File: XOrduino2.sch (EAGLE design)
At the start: 82 parts, among them J1 2.5mm, J2 2.5mm, J3 2.5mm, J4 2.5mm, J5 Batt In, J6 MOT R, J7 MOT L, P1 10k, Q1 ALS-PT204-6C/L177, SW1 RESET, SW2 6mm Button, SW3 LEFT BUMPER, SW4 RIGHT BUMPER, U1 ATMEGA32U4-XUAU, U2 LMV358, U3 NJU7261, U4 DRV8833PWP, U5 QRE1113GR, U6 QRE1113GR, X1 USBPCB, X2 USBMINIB, X3 USBMICROB-VIA, Y1 16MHz

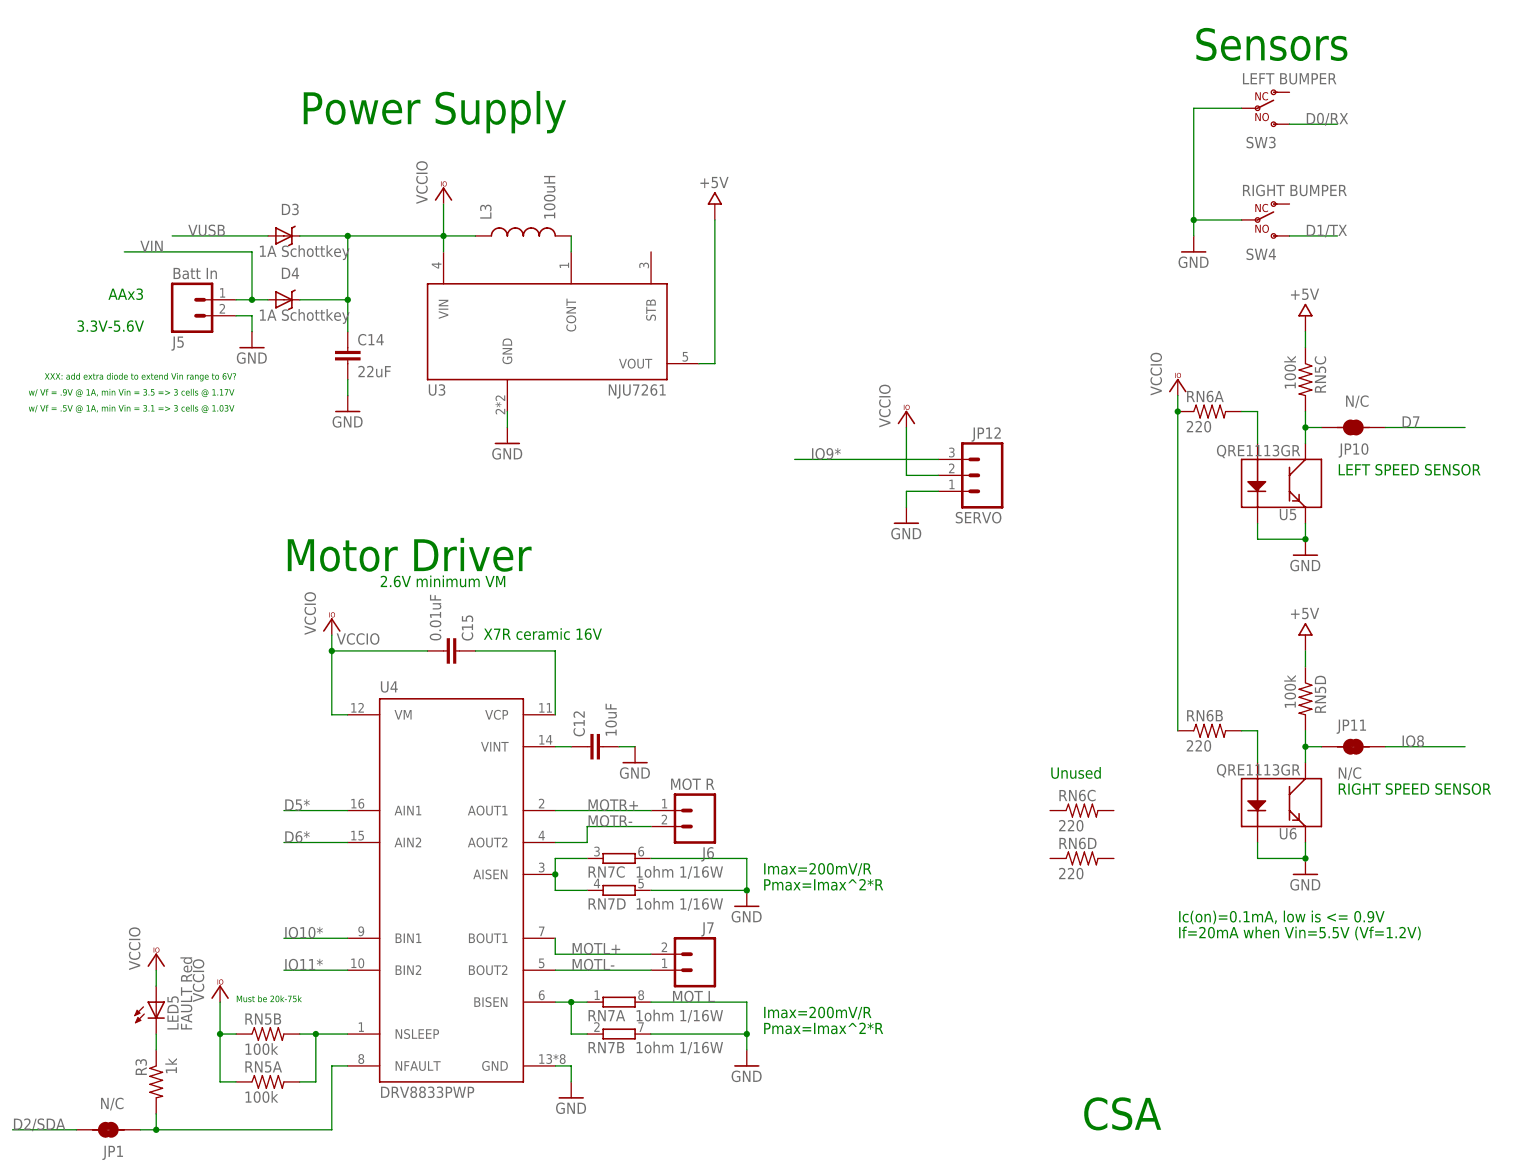
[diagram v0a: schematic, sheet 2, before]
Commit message: all of second page deleted
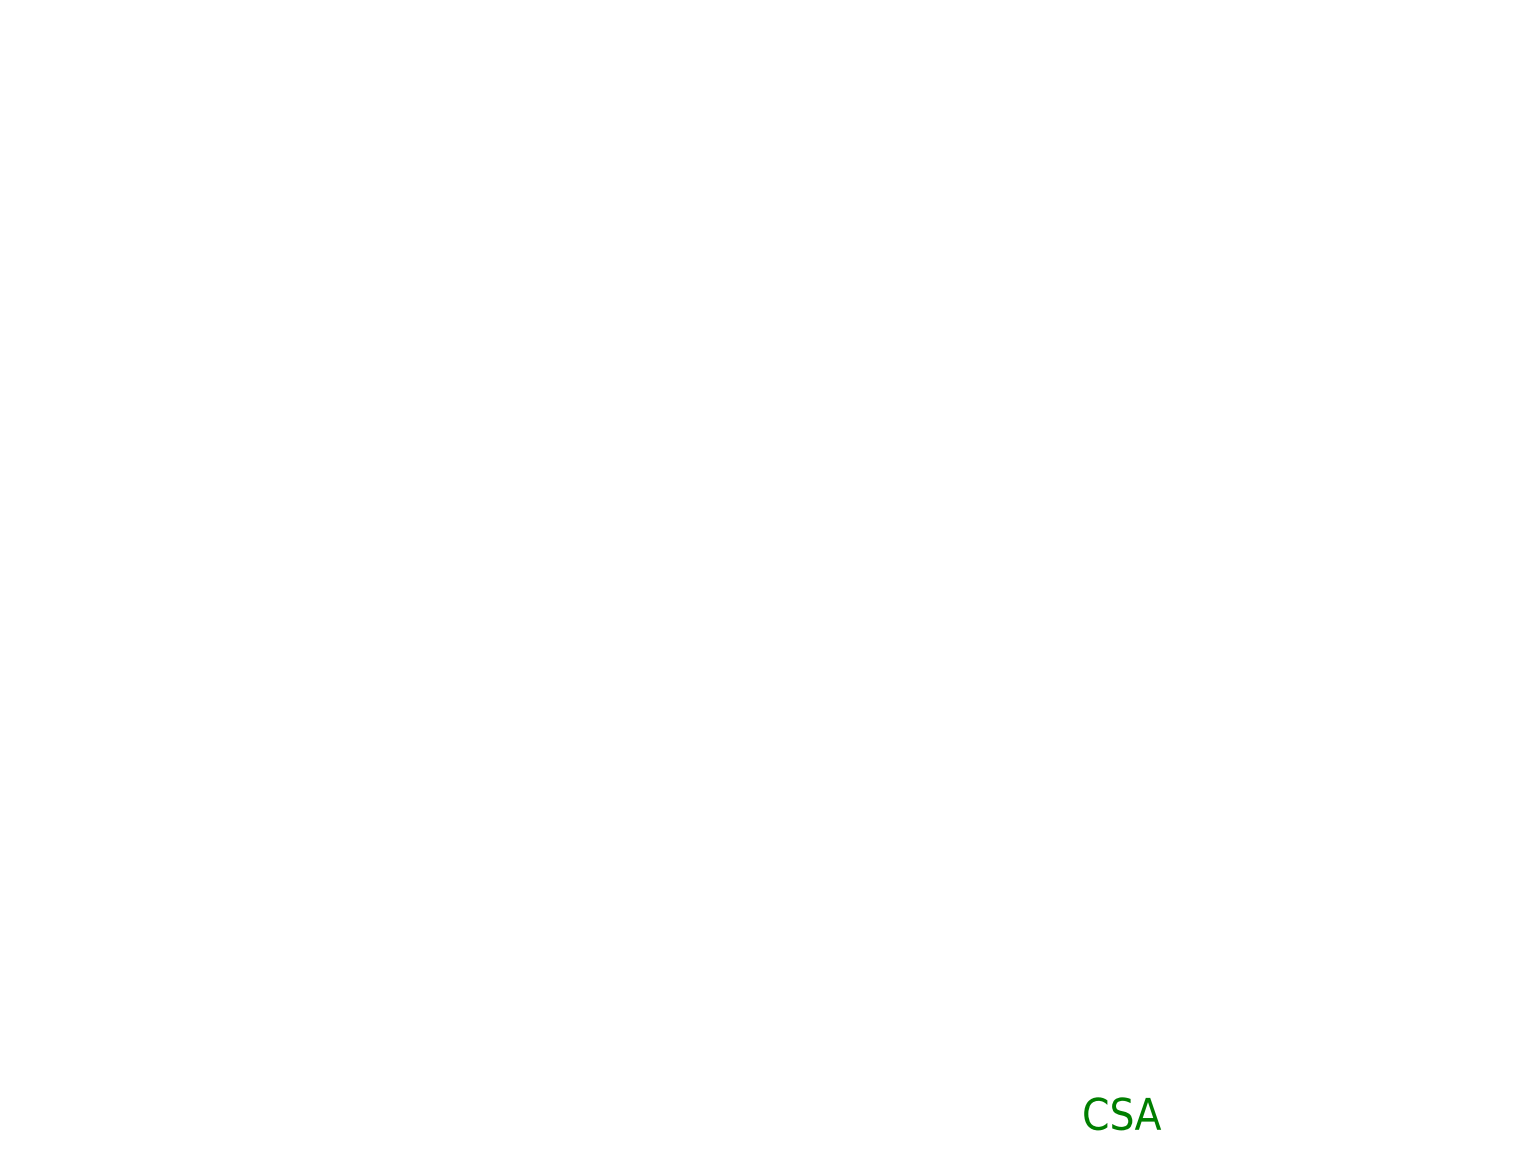
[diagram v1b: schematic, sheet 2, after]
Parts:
- removed C10: 0.22uF, SparkFun-Passives:CAP0805
- removed C11: 0.33uF, SparkFun-Passives:CAP0805
- removed C12: 10uF, SparkFun-Passives:CAP0805
- removed C14: 22uF, SparkFun-Passives:CAP1206
- removed C15: 0.01uF, SparkFun-Passives:CAP0805
- removed C7: 100n, SparkFun-Passives:CAP0805
- removed D1: 1N4148, SparkFun-DiscreteSemi:DIODE1N4148
- removed D3, D4: 1A Schottkey, SparkFun-DiscreteSemi:DIODE-SCHOTTKY_
- removed J1, J2, J3, J4: 2.5mm, xorduino:AUDIO-JACK
- removed J5: Batt In, SparkFun-Connectors:M02PTH
- removed J6: MOT R, SparkFun:M023.5MM
- removed J7: MOT L, SparkFun:M023.5MM
- removed JP1: N/C, xorduino:SOLDERJUMPERNOCONFLICT
- removed JP10, JP11: N/C, xorduino:SOLDERJUMPERBOT-VIA-NOCONFLICT
- removed JP12: SERVO, SparkFun-Connectors:M03PTH
- removed L3: 100uH, SparkFun-Passives:INDUCTOR1007
- removed LED5: FAULT Red, xorduino:LED0805
- removed MIC1: MIC9.7MM, SparkFun:MIC9.7MM
- removed P1: 10k, xorduino:POT
- removed Q1: ALS-PT204-6C/L177, xorduino:ALS-PT204-6C/L177
- removed R2: 2.2k, SparkFun-Passives:RESISTOR0805-RES
- removed R3: 1k, SparkFun-Passives:RESISTOR0805-RES
- removed RN5: 100k, xorduino:RESISTOR-ARRAYCRA06S
- removed RN6: 220, xorduino:RESISTOR-ARRAYCRA06S
- removed RN7: 1ohm 1/16W, resistor-dil:4R-NEXB38V
- removed SW2: 6mm Button, SparkFun-Electromechanical:TAC_SWITCHPTH
- removed SW3: LEFT BUMPER, xorduino:SWITCH-SPDTV1-NOHOLES
- removed SW4: RIGHT BUMPER, xorduino:SWITCH-SPDTV2-NOHOLES
- removed U3: NJU7261, xorduino:NJU7261
- removed U4: DRV8833PWP, xorduino:DRV8833PWP
- removed U5, U6: QRE1113GR, xorduino:QRE1113GR
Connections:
- removed net LED5_CATHODE: LED5.C, R3.1
- removed net MIC_IN: C7.1, MIC1.1, RN2B.1
- removed net MOTL+: J7.2, U4.BOUT1
- removed net MOTL-: J7.1, U4.BOUT2
- removed net MOTR+: J6.1, U4.AOUT1
- removed net MOTR-: J6.2, U4.AOUT2
- removed net OPAMP1_M: R2.2, RN4C.2, U2G$2.-IN2
- removed net OPAMP1_OUT: D1.A, RN4C.1, U2G$2.OUT2
- removed net OPAMP1_P: C7.2, RN2C.2, U2G$2.+IN2
- removed net U3_CONT: L3.2, U3.CONT
- removed net U4_AISEN: RN7C.1, RN7D.1, U4.AISEN
- removed net U4_BISEN: RN7A.1, RN7B.1, U4.BISEN
- removed net U4_NFAULT: JP1.1, R3.2, U4.NFAULT
- removed net U4_NSLEEP: RN5A.2, RN5B.2, U4.NSLEEP
- removed net U4_VCP: C15.1, U4.VCP
- removed net U4_VINT: C12.1, U4.VINT
- removed net U5_ANODE: RN6A.2, U5.A
- removed net U5_COLLECTOR: JP10.2, RN5C.2, U5.C
- removed net U6_ANODE: RN6B.2, U6.A
- removed net U6_COLLECTOR: JP11.1, RN5D.2, U6.C
- removed net VCCIO: C14.1, C15.2, D3.C, D4.C, JP12.2, L3.1, LED5.A, RN5A.1, RN5B.1, RN6A.1, RN6B.1, U3.VIN, U4.VM
- net +5V: no longer C11.1, P1.E, RN2B.2, RN4D.2, RN5C.1, RN5D.1, U3.VOUT
- net A0: no longer J1.TIP
- net A1: no longer J2.TIP
- net A2: no longer J3.TIP
- net A3: no longer J4.TIP
- net D0/RX: no longer SW3.NO
- net D1/TX: no longer SW4.NO
- net D2/SDA: no longer JP1.2
- net D5*: no longer U4.AIN1
- net D6*: no longer U4.AIN2
- net D7: no longer JP10.1
- net GND: no longer C10.1, C12.2, C14.2, J1.SLEEVE, J2.SLEEVE, J3.SLEEVE, J4.SLEEVE, J5.2, JP12.1, MIC1.2, P1.A, Q1.E1, R2.1, RN2C.1, RN4B.2, RN7A.2, RN7B.2, RN7C.2, RN7D.2, SW2.4, SW3.C, SW4.C, U3.GND, U4.GND, U5.E, U5.K, U6.E, U6.K
- net IO10*: no longer U4.BIN1
- net IO11*: no longer U4.BIN2
- net IO12: no longer SW2.1
- net IO8: no longer JP11.2
- net IO9*: no longer JP12.3
- net LIGHT: no longer C11.2, Q1.C1, RN4D.1
- net SLIDER: no longer P1.S
- net SOUND: no longer C10.2, D1.C, RN4B.1
- net VIN: no longer D4.A, J5.1
- net VUSB: no longer D3.A
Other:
- note removed: "2.6V minimum VM"
- note removed: "3.3V-5.6V"
- note removed: "A"
- note removed: "AAx3"
- note removed: "All components optional"
- note removed: "B"
- note removed: "C"
- note removed: "D"
- note removed: "Ic(on)=0.1mA, low is <= 0.9V"
- note removed: "If=20mA when Vin=5.5V (Vf=1.2V)"
- note removed: "Imax=200mV/R"
- note removed: "LEFT SPEED SENSOR"
- note removed: "LMV358"
- note removed: "Motor Driver"
- note removed: "Must be 20k-75k"
- note removed: "Pmax=Imax^2*R"
- note removed: "Power Supply"
- note removed: "RIGHT SPEED SENSOR"
- note removed: "Scratch Sensor Board"
- note removed: "Sensors"
- note removed: "X7R ceramic 16V"
- note removed: "XXX: add extra diode to extend Vin range to 6V?"
- note removed: "w/ Vf = .5V @ 1A, min Vin = 3.1 => 3 cells @ 1.03V"
- note removed: "w/ Vf = .9V @ 1A, min Vin = 3.5 => 3 cells @ 1.17V"

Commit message: most of un-needed items removed. Current sense mostly in place
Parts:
- removed H1: 10x1F-H8.5, SmartPrj:PINHD-1X10
- removed H2, H3: 8x1F-H8.5, SmartPrj:PINHD-1X8
- removed H4: 6x1F-H8.5, SmartPrj:PINHD-1X6
- removed JP5: N/C, xorduino:SOLDERJUMPERNOCONFLICT
- removed JP7, JP8: N/C, xorduino:SOLDERJUMPERBOT-VIA-NOCONFLICT
- removed JP9: N/C, xorduino:SOLDERJUMPERBOT-NOCONFLICT
- removed LED1: L Yellow, xorduino:LED0805
- removed U$5: OSHW-LOGOL, SparkFun-Aesthetics:OSHW-LOGOL
- removed X1: USBPCB, SparkFun-Connectors:USBPCB
- removed X2: USBMINIB, xorduino:USBMINIB
- U2: value LMV358 -> LCD-16X2SILK; device SparkFun:LMV358 -> SparkFun-Displays:LCD-16X2SILK
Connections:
- removed net +3V3: H3.4
- removed net IO13_MIRROR: JP5.2, RN3A.2, U2G$1.-IN1, U2G$1.OUT1
- removed net LED1_ANODE: LED1.A, RN3A.1
- removed net LIGHT: JP8.1
- removed net SLIDER: JP9.1
- removed net SOUND: JP7.1
- removed net VIN: H3.8
- net +5V: no longer H3.2, H3.5, U2G$1.+V
- net A0: no longer H4.1
- net A1: no longer H4.2
- net A2: no longer H4.3
- net A3: no longer H4.4
- net A4: no longer H4.5, JP7.2
- net A5: no longer H4.6, JP8.2
- net AREF: no longer H1.8
- net D0/RX: no longer H2.1
- net D1/TX: no longer H2.2
- net D2/SDA: no longer H1.9, H2.3
- net D3/SCL: no longer H1.10, H2.4
- net D4: no longer H2.5, JP9.2
- net D5*: no longer H2.6
- net D6*: no longer H2.7
- net D7: no longer H2.8
- net D_M: no longer X1.D-, X2.D-
- net D_P: no longer X1.D+, X2.D+
- net GND: no longer H1.7, H3.6, H3.7, LED1.C, U2G$1.GND
- net IO10*: no longer H1.3
- net IO11*: no longer H1.4
- net IO12: no longer H1.5
- net IO13*: no longer H1.6, JP5.1, U2G$1.+IN1
- net IO8: no longer H1.1
- net IO9*: no longer H1.2
- net RESET: no longer H3.3
- net UGND: no longer X1.GND, X2.GND
- net XUSB: no longer X1.VBUS, X2.VBUS
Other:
- note removed: "#PWM 10bit"
- note removed: "#PWM 16bit"
- note removed: "#PWM 8/16bit"
- note removed: "#PWM 8bit"
- note removed: "#PWM Hi-Speed"
- note removed: "+A10"
- note removed: "+A11"
- note removed: "+A6"
- note removed: "+A7"
- note removed: "+A8"
- note removed: "+A9"
- note removed: "+AIN0"
- note removed: "+PWM COMPL IO10"
- note removed: "10#"
- note removed: "11#"
- note removed: "3#"
- note removed: "5#"
- note removed: "6#"
- note removed: "9#"
- note removed: "ALT1"
- note removed: "ALT2"
- note removed: "ALT3"
- note removed: "Cut jumper if U2 populated"
- note removed: "IO"
- note removed: "IOREF"
- note removed: "PWM 16bit COMPL D6"
- note removed: "RFU"
- note removed: "TO ICSP"

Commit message: starting to eliminate vias, work with component orientation
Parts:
- removed D2: 1N4148, SparkFun-DiscreteSemi:DIODE1N4148
- removed F1: 0ZCC0110FF2C 1.1A, rcl:L-EUL1812
- removed JP2, JP3, JP4, JP6: N/C, xorduino:SOLDERJUMPERNOCONFLICT
- removed LED2: TX Red, xorduino:LED0805
- removed LED3: RX Red, xorduino:LED0805
- added Q1: 2N2907, adafruit:2N2907
- added R2, R3, R5, R6: (no value), SparkFun-Passives:RESISTOR1206
- added RN5: 22, xorduino:RESISTOR-ARRAYCRA06S
- added SW2: RESET, SparkFun-Electromechanical:TAC_SWITCHPTH
- added U$2: LMV358, SparkFun-AnalogIC:LMV358
- added U$5: MMDT3904, SparkFun-DiscreteSemi:MMDT3904
- added U$6: RJ45-8PTH, SparkFun-Connectors:RJ45-8PTH
- added U$8: LM2931_FIXED, SparkFun-PowerIC:LM2931_FIXED
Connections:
- removed net VUSB: F1.1, JP6.1, U1.VBUS
- removed net XUSB: F1.2, X3.VBUS
- new net N$1: RN5D.2, U$2G$1.+IN1, U$5G$1.C
- new net N$12: R5.2, U2.VO
- new net N$13: U2.A
- new net N$14: Q1.B, R6.2
- new net N$18: U$6.2, U$8.VIN
- new net N$2: RN5A.2, U$2G$2.-IN2
- new net N$3: RN5B.2, U$2G$2.+IN2, U$5G$2.C
- new net N$4: U$2G$1.OUT1, U$5G$1.B
- new net N$5: U$2G$2.OUT2, U$5G$2.B
- new net N$6: RN5C.2, U$2G$1.-IN1
- new net N$7: RN5A.1, RN5D.1, U$6.8
- new net N$8: RN5B.1, RN5C.1, U$6.7
- net +5V: now also Q1.E, U$8.VOUT, U1.VBUS, U2.VDD, X3.VBUS; no longer D2.C, JP2.1, JP6.2
- net A0: now also R3.2, U$5G$2.E
- net A1: now also R2.2, U$5G$1.E
- net AGND: no longer C6.1, JP3.1
- net AVCC: no longer JP2.2
- net D0/RX: now also U2.DB5
- net D1/TX: now also U2.DB4
- net D2/SDA: now also U2.DB6
- net D3/SCL: now also U2.DB7
- net GND: now also C6.1, R2.1, R3.1, R5.1, U$6.1, U$8.GND, U2.K, U2.R/W, U2.VSS; no longer JP3.2, JP4.1
- net LED2_ANODE: no longer LED2.A
- net LED3_ANODE: no longer LED3.A
- net RESET: no longer D2.A
- net RXLED: no longer LED3.C
- net TXLED: no longer LED2.C
- net UGND: no longer JP4.2
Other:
- note added: "Battery Monitor"
- note removed: "0"
- note removed: "1"
- note removed: "10"
- note removed: "11"
- note removed: "12"
- note removed: "13"
- note removed: "2"
- note removed: "3"
- note removed: "4"
- note removed: "5"
- note removed: "6"
- note removed: "7"
- note removed: "9"
- note removed: "XOrduino2 (leonardo-compatible)"
- moved on the sheet: L2, RN1A, RN1B, RN1C, RN1D, RN4A, Z1, Z2

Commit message: changed usb connector, most of the devices are connected
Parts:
- removed R3: (no value), SparkFun-Passives:RESISTOR1206
- removed RN4: 100k, xorduino:RESISTOR-ARRAYCRA06S
- removed X3: USBMICROB-VIA, xorduino:USBMICROB-VIA
- added JP1: USB-RECEPTABLE, daspilker:USB-RECEPTABLE
- added R4, R7: (no value), SparkFun-Passives:RESISTOR0805-RES
- added RN6: 10k, xorduino:RESISTOR-ARRAYCRA06S
- R2: device SparkFun-Passives:RESISTOR1206 -> SparkFun-Passives:RESISTOR0805-RES
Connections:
- removed net A1: R2.2, U$5G$1.E, U1.(ADC6/TDO)PF6
- removed net LED2_ANODE: RN3C.1
- new net N$11: R2.1, RN3C.2, U1.(ADC7/TDI)PF7
- new net N$15: JP1.ID
- new net N$9: U1.(ADC5/TMS)PF5
- net +5V: now also JP1.VCC, RN6A.2, RN6B.2; no longer RN2A.2, RN3C.2, X3.VBUS
- net A0: now also R7.2, U1.(ADC6/TDO)PF6; no longer R3.2, U1.(ADC7/TDI)PF7
- net A2: now also R4.2, U$5G$1.E; no longer U1.(ADC5/TMS)PF5
- net D7: now also RN6B.1, SW2.4
- net D_M: now also JP1.D-, RN1D.2; no longer RN1C.2, X3.D-
- net D_P: now also JP1.D+, RN1C.2; no longer RN1D.2, X3.D+
- net GND: now also R4.1, R7.1, RN3C.1, SW2.2; no longer R2.1, R3.1
- net N$7: now also R2.2
- net RD_M: now also RN1D.1; no longer RN1C.1
- net RD_P: now also RN1C.1; no longer RN1D.1
- net RESET: now also RN6A.1; no longer RN2A.1
- net UGND: now also JP1.GND; no longer X3.GND
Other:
- note removed: "Cut for Battery Power Option"
- moved on the sheet: C8, L2, R2, RN1C, RN1D, RN3C, Z1, Z2

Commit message: added terminal block to sense power on
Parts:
- removed RN2: 10k, xorduino:RESISTOR-ARRAYCRA06S
- added C10, C7: (no value), SparkFun-Capacitors:CAP0805
- added R3: (no value), adafruit:R-US_0207/15
- added X1: (no value), con-wago-508:W237-03P
- RN5: value 22 -> 1K
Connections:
- new net N$10: Q1.C, R3.1
- new net N$16: U1.VBUS
- new net N$20: U$6.5
- net +5V: now also U$2G$1.+V; no longer U1.VBUS
- net A0: now also C10.1
- net A2: now also C7.1
- net GND: now also C10.2, C7.2, RN6C.1, RN6D.1, U$6.3, U$6.4; no longer R5.1, RN2D.1, RN3C.1
- net HWB: now also RN6D.2; no longer RN2D.2
- net IO10*: now also U$6.6
- net N$11: now also RN6C.2; no longer RN3C.2
- net N$13: now also R3.2
- net N$14: now also R6.1
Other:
- moved on the sheet: JP1, Q1, R2, R5, R6, RN1C, RN1D, RN3C, RN6C, RN6D, U$6, U$8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

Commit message: some hand routing, currently about4 air wires
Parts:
- removed RN3: 1k, xorduino:RESISTOR-ARRAYCRA06S
- added R8: 47k, SparkFun-Passives:RESISTOR0805-RES
- added RN2: 1k, xorduino:RESISTOR-ARRAYCRA06S
- Q1: value 2N2907 -> TRANSISTOR_PNPTO92; device adafruit:2N2907 -> SparkFun-DiscreteSemi:TRANSISTOR_PNPTO92
- R2: value (none) -> 22k
- R3: value (none) -> 47
- R4, R7: value (none) -> 47k
- R5, R6: value (none) -> 47k; device SparkFun-Passives:RESISTOR1206 -> SparkFun-Passives:RESISTOR0805-RES
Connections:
- removed net LED3_ANODE: RN3D.1
- removed net N$14: Q1.B, R6.1, R6.2
- new net D6: U2.E
- new net N$19: Q1.B, RN2A.1
- net +5V: now also RN2B.2, X1-1.KL; no longer RN3B.2, RN3D.2
- net A0: now also R8.2
- net A2: now also R6.2
- net D0/RX: now also U2.DB4; no longer U2.DB5
- net D1/TX: now also U2.DB5; no longer U2.DB4
- net D7: now also U2.RS
- net GND: now also R5.1, R6.1, R8.1, X1-3.KL
- net IO10*: now also X1-2.KL
- net IO8: now also RN2A.2
- net LED4_ANODE: now also RN2B.1; no longer RN3B.1
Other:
- moved on the sheet: R5, R6
